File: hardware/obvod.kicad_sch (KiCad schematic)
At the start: 1 part

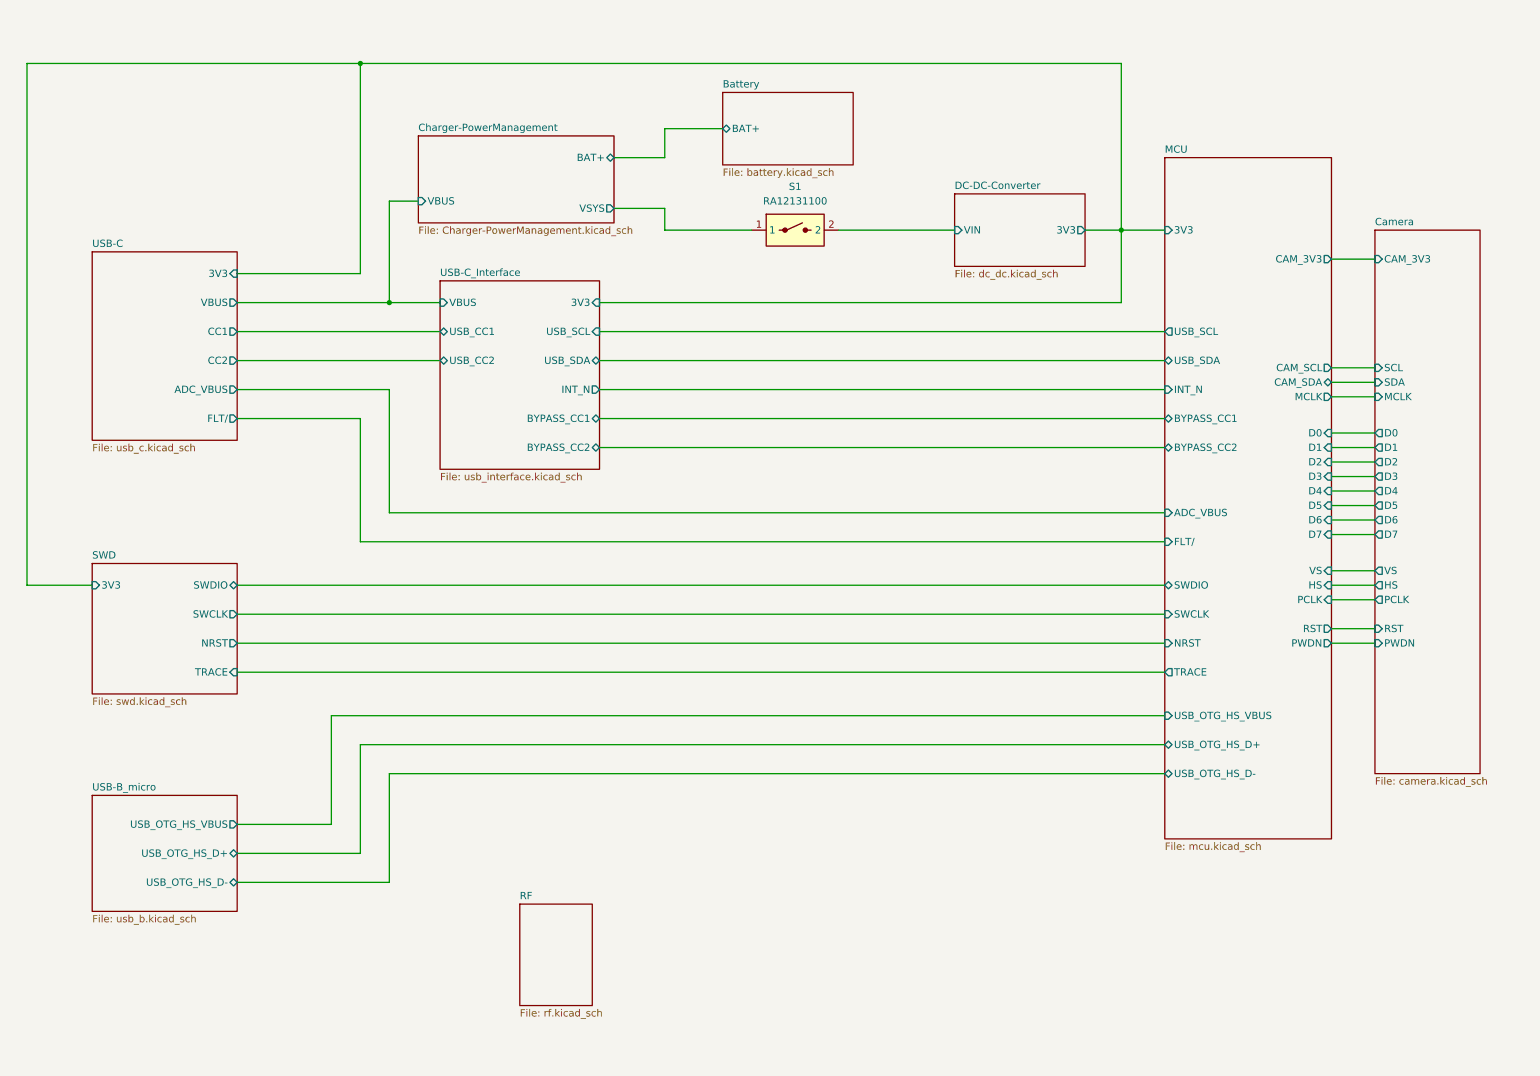
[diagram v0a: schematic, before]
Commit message: Battery temperature meter added to MCU
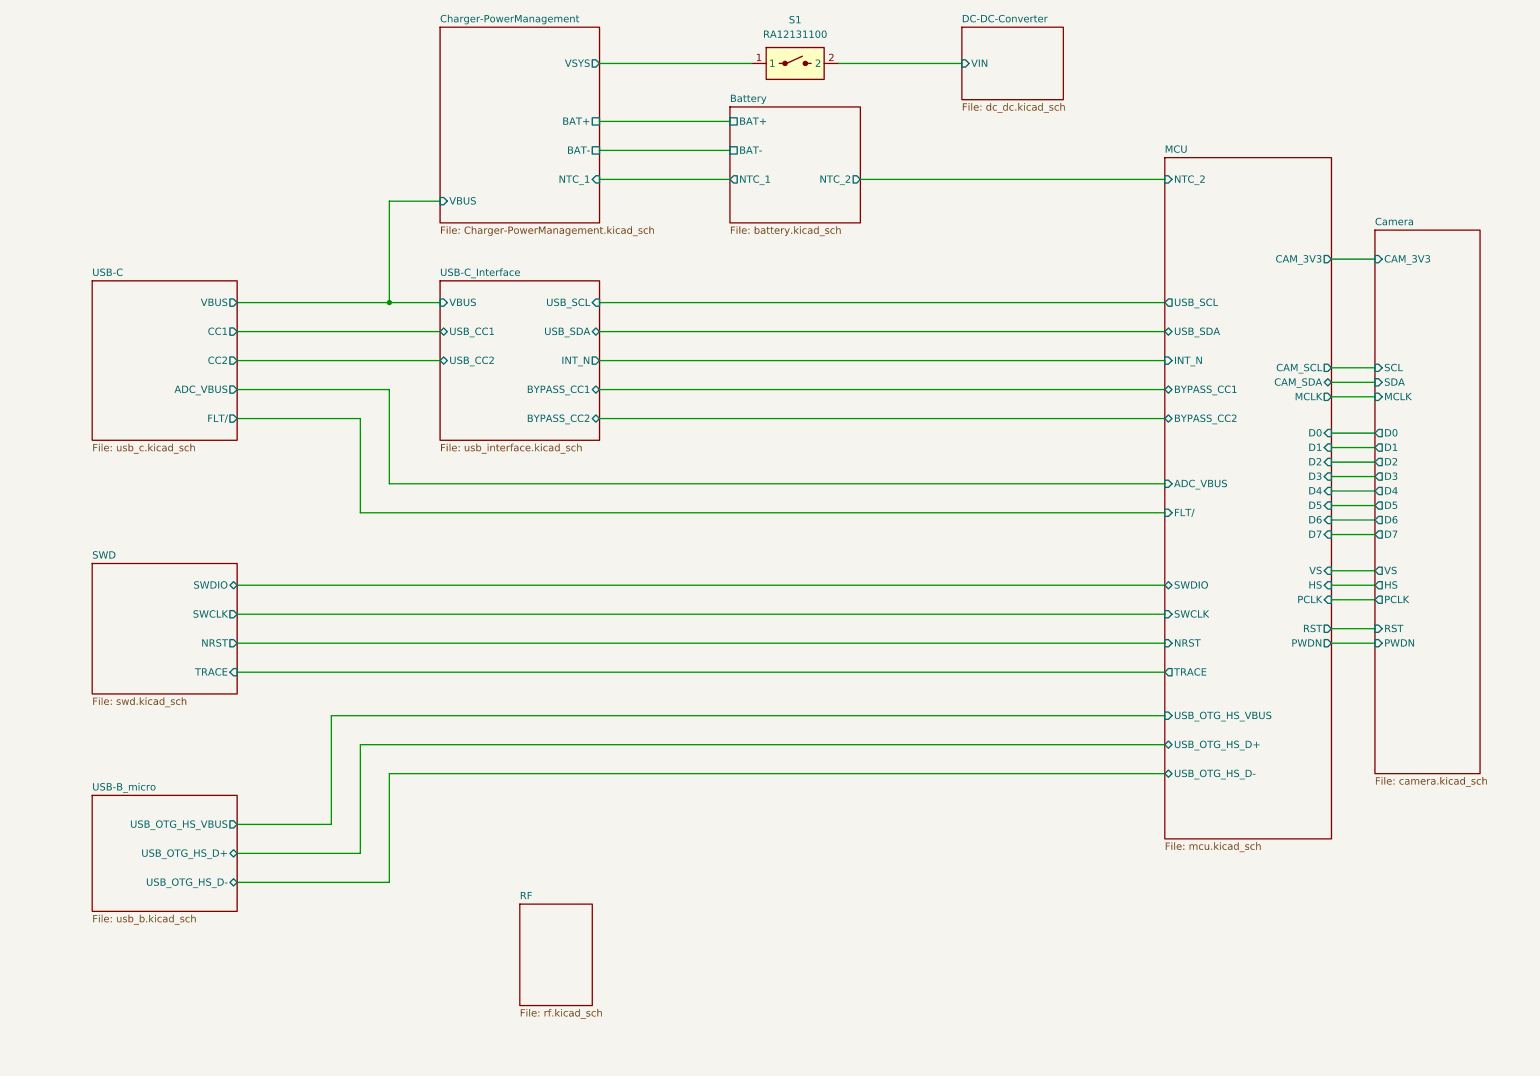
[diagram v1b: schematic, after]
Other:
- sheet Battery ports: added BAT-, NTC_1, NTC_2; removed none
- sheet Charger-PowerManagement ports: added BAT-, NTC_1; removed none
- sheet DC-DC-Converter ports: added none; removed 3V3
- sheet MCU ports: added NTC_2; removed 3V3
- sheet SWD ports: added none; removed 3V3
- sheet USB-C ports: added none; removed 3V3
- sheet USB-C_Interface ports: added none; removed 3V3
- moved on the sheet: S1

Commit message: Done?
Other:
- sheet MCU ports: added COMMAND_DONE, SCLK, SDI, SDO, nIRQ, nSEL; removed none
- sheet RF ports: added COMMAND_DONE, SCLK, SDI, SDO, nIRQ, nSEL; removed none

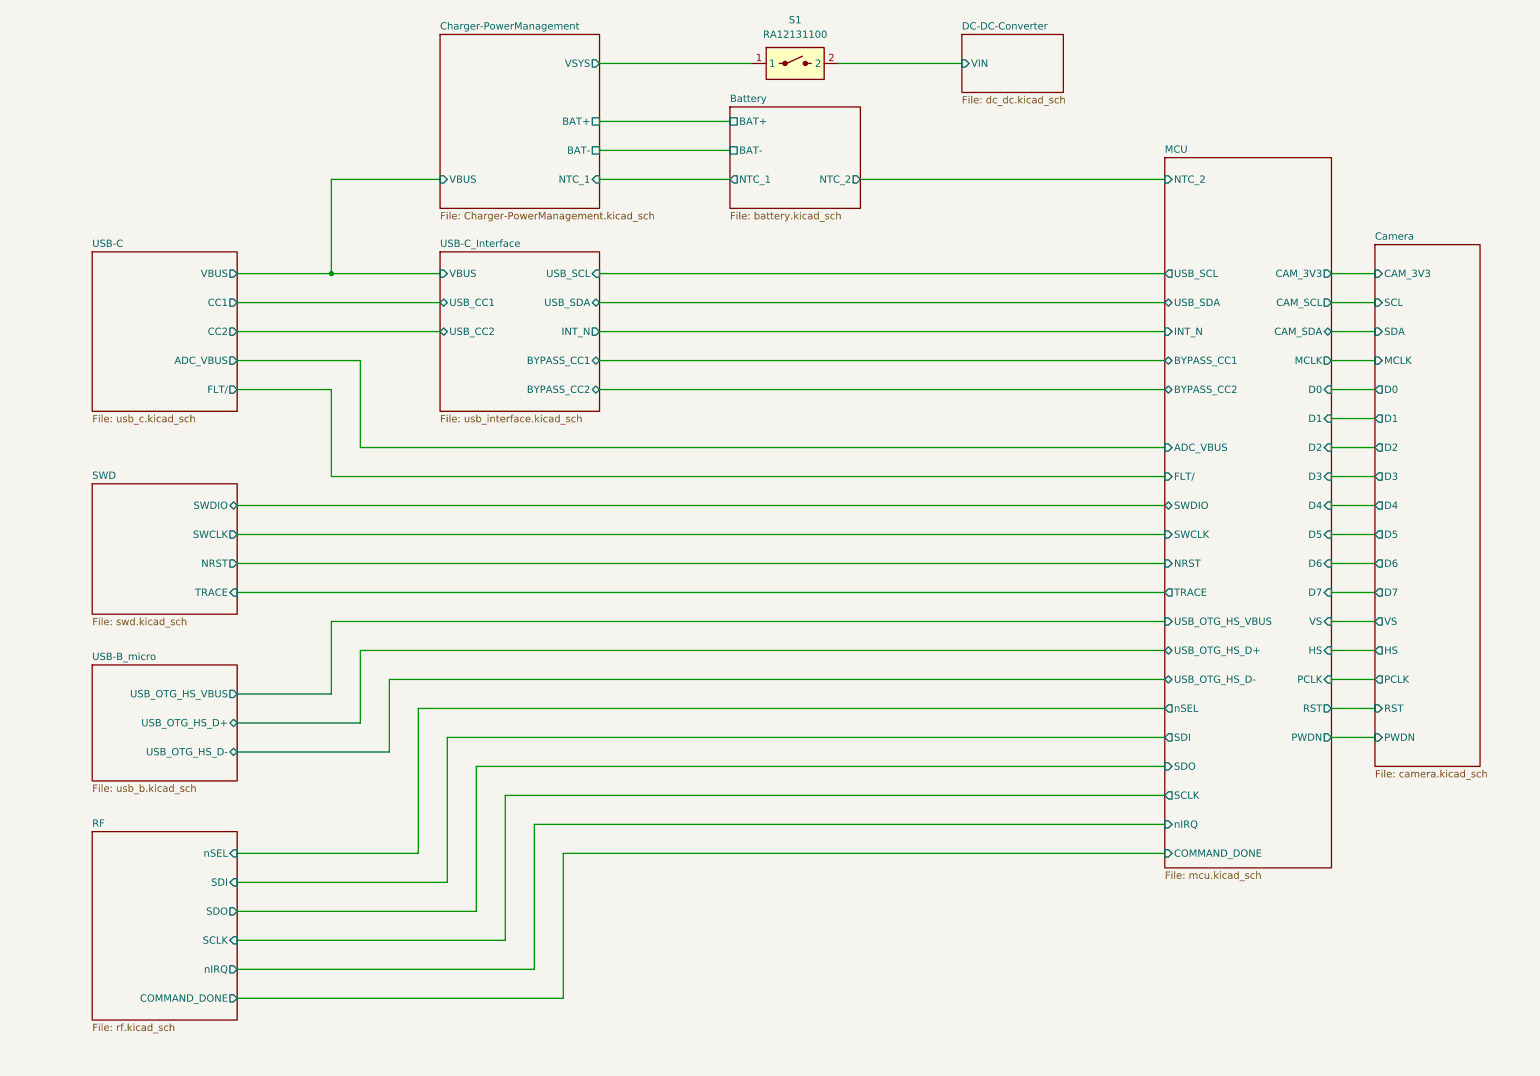
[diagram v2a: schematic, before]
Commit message: Board connector added
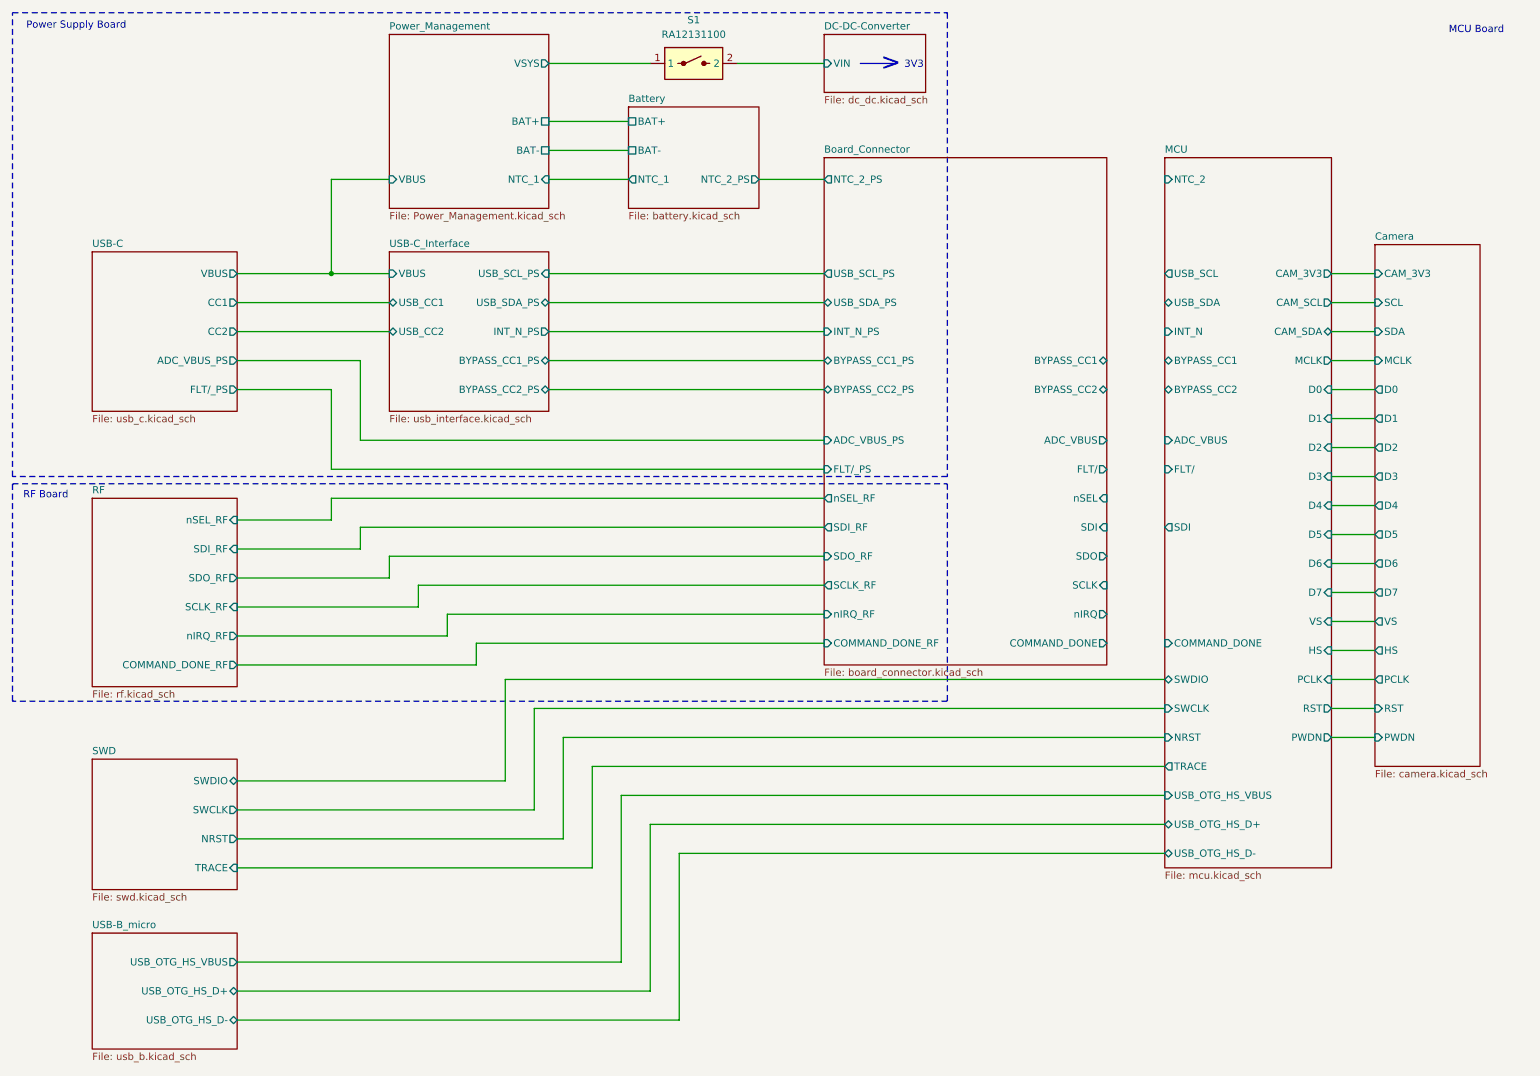
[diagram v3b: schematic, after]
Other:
- sheet Charger-PowerManagement renamed Power_Management
- added sheet Board_Connector (board_connector.kicad_sch)
- sheet Battery ports: added NTC_2_PS; removed NTC_2
- sheet MCU ports: added none; removed SCLK, SDO, nIRQ, nSEL
- sheet Power_Management: file Charger-PowerManagement.kicad_sch -> Power_Management.kicad_sch
- sheet RF ports: added COMMAND_DONE_RF, SCLK_RF, SDI_RF, SDO_RF, nIRQ_RF, nSEL_RF; removed COMMAND_DONE, SCLK, SDI, SDO, nIRQ, nSEL
- sheet USB-C ports: added ADC_VBUS_PS, FLT/_PS; removed ADC_VBUS, FLT/
- sheet USB-C_Interface ports: added BYPASS_CC1_PS, BYPASS_CC2_PS, INT_N_PS, USB_SCL_PS, USB_SDA_PS; removed BYPASS_CC1, BYPASS_CC2, INT_N, USB_SCL, USB_SDA
- note added: "3V3"
- note added: ">"
- note added: "MCU Board"
- note added: "Power Supply Board"
- note added: "RF Board"
- moved on the sheet: S1

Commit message: prevention save
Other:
- sheet Board_Connector ports: added INT_N, NTC_2, USB_SCL, USB_SDA; removed none
- sheet MCU ports: added SCLK, SDO, nIRQ, nSEL; removed none
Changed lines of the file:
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@@
+	(wire
+		(pts
+			(xy 210.82 87.63) (xy 220.98 87.63)
+		)
+		(stroke
+			(width 0)
+			(type default)
+		)
+	)
 	(wire
 		(pts
@@
 	(wire
 		(pts
+			(xy 210.82 68.58) (xy 220.98 68.58)
+		)
+		(stroke
+			(width 0)
+			(type default)
+		)
+	)
+	(wire
+		(pts
 			(xy 135.89 160.02) (xy 135.89 189.23)
 		)
@@
 	(wire
 		(pts
+			(xy 210.82 58.42) (xy 220.98 58.42)
+		)
+		(stroke
+			(width 0)
+			(type default)
+		)
+	)
+	(wire
+		(pts
 			(xy 120.65 144.78) (xy 220.98 144.78)
 		)
@@
 	(wire
 		(pts
+			(xy 210.82 92.71) (xy 220.98 92.71)
+		)
+		(stroke
+			(width 0)
+			(type default)
+		)
+	)
+	(wire
+		(pts
 			(xy 58.42 116.84) (xy 90.17 116.84)
 		)
@@
 	(wire
 		(pts
+			(xy 210.82 73.66) (xy 220.98 73.66)
+		)
+		(stroke
+			(width 0)
+			(type default)
+		)
+	)
+	(wire
+		(pts
+			(xy 210.82 102.87) (xy 220.98 102.87)
+		)
+		(stroke
+			(width 0)
+			(type default)
+		)
+	)
+	(wire
+		(pts
 			(xy 80.01 106.68) (xy 80.01 102.87)
 		)
@@
 	(wire
 		(pts
+			(xy 210.82 41.91) (xy 220.98 41.91)
+		)
+		(stroke
+			(width 0)
+			(type default)
+		)
+	)
+	(wire
+		(pts
 			(xy 113.03 21.59) (xy 130.81 21.59)
 		)
@@
 	(wire
 		(pts
+			(xy 210.82 63.5) (xy 220.98 63.5)
+		)
+		(stroke
+			(width 0)
+			(type default)
+		)
+	)
+	(wire
+		(pts
 			(xy 130.81 154.94) (xy 130.81 184.15)
 		)
@@
 	(wire
 		(pts
+			(xy 210.82 107.95) (xy 220.98 107.95)
+		)
+		(stroke
+			(width 0)
+			(type default)
+		)
+	)
+	(wire
+		(pts
 			(xy 130.81 154.94) (xy 220.98 154.94)
 		)
@@
 	(wire
 		(pts
+			(xy 210.82 123.19) (xy 220.98 123.19)
+		)
+		(stroke
+			(width 0)
+			(type default)
+		)
+	)
+	(wire
+		(pts
 			(xy 125.73 179.07) (xy 58.42 179.07)
 		)
@@
 	(wire
 		(pts
+			(xy 210.82 113.03) (xy 220.98 113.03)
+		)
+		(stroke
+			(width 0)
+			(type default)
+		)
+	)
+	(wire
+		(pts
 			(xy 80.01 87.63) (xy 161.29 87.63)
 		)
@@
 	(wire
 		(pts
+			(xy 210.82 78.74) (xy 220.98 78.74)
+		)
+		(stroke
+			(width 0)
+			(type default)
+		)
+	)
+	(wire
+		(pts
+			(xy 210.82 97.79) (xy 220.98 97.79)
+		)
+		(stroke
+			(width 0)
+			(type default)
+		)
+	)
+	(wire
+		(pts
 			(xy 74.93 101.6) (xy 74.93 97.79)
 		)
@@
 		(pts
 			(xy 250.19 68.58) (xy 257.81 68.58)
+		)
+		(stroke
+			(width 0)
+			(type default)
+		)
+	)
+	(wire
+		(pts
+			(xy 210.82 118.11) (xy 220.98 118.11)
 		)
 		(stroke
@@
 			)
 		)
+		(pin "nSEL" output
+			(at 220.98 97.79 180)
+			(effects
+				(font
+					(size 1.27 1.27)
+				)
+				(justify left)
+			)
+		)
+		(pin "nIRQ" input
+			(at 220.98 118.11 180)
+			(effects
+				(font
+					(size 1.27 1.27)
+				)
+				(justify left)
+			)
+		)
+		(pin "SDO" input
+			(at 220.98 107.95 180)
+			(effects
+				(font
+					(size 1.27 1.27)
+				)
+				(justify left)
+			)
+		)
+		(pin "SCLK" output
+			(at 220.98 113.03 180)
+			(effects
+				(font
+					(size 1.27 1.27)
+				)
+				(justify left)
+			)
+		)
 		(instances
 			(project "obvod"
@@
 			(effects
 				(font
+					(size 1.27 1.27)
+				)
+				(justify right)
+			)
+		)
+		(pin "NTC_2" output
+			(at 210.82 41.91 0)
+			(effects
+				(font
+					(size 1.27 1.27)
+				)
+				(justify right)
+			)
+		)
+		(pin "USB_SDA" bidirectional
+			(at 210.82 63.5 0)
+			(effects
+				(font
+					(size 1.27 1.27)
+				)
+				(justify right)
+			)
+		)
+		(pin "USB_SCL" input
+			(at 210.82 58.42 0)
+			(effects
+				(font
+					(size 1.27 1.27)
+				)
+				(justify right)
+			)
+		)
+		(pin "INT_N" output
+			(at 210.82 68.58 0)
+			(effects
+				(font
